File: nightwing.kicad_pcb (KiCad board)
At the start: 2 copper layers, 165.4 x 129.6 mm, 109 parts, among them J1 USB_C_Receptacle_USB2.0, J2 USB_C_Receptacle_USB2.0, J3 OLED, SW1 SW_PUSH, SW10 SW_PUSH, SW11 SW_PUSH, SW12 SW_PUSH, SW13 SW_PUSH, SW14 SW_PUSH, SW15 SW_PUSH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

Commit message: updated stm32
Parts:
- added G***: LOGO, private:tiny_nightwing, F.Cu at (37.1, 38.7)
- added G***: LOGO, private:icon_nightwing, F.Cu at (156.2, 87.4)
- added L40: WS2812B, reversible-kicad-footprints:ws2812_reversible, B.Cu at (86.9, 86.4)
- added L41: WS2812B, reversible-kicad-footprints:ws2812_reversible, B.Cu at (102.1, 31.0)
- added L42: WS2812B, reversible-kicad-footprints:ws2812_reversible, B.Cu at (66.0, 25.1)
- J2: moved to F.Cu
- moved RESET_SW1 33.5 mm to (139.6, 89.2)
- moved C1 28.1 mm to (149.1, 86.0), turned to 270 degrees
- moved R5 27.0 mm to (159.1, 81.5), turned to 0 degrees
- moved R7 25.8 mm to (159.1, 79.4), turned to 0 degrees
- moved C10 25.2 mm to (159.1, 77.3), turned to 0 degrees
- moved C5 20.4 mm to (136.2, 76.7), turned to 180 degrees
- moved R2 20.1 mm to (136.2, 72.6), turned to 0 degrees
- moved L37 17.6 mm to (150.0, 103.2)
- moved J2 13.5 mm to (171.8, 106.2), turned to 170 degrees
- moved U1 12.4 mm to (28.5, 26.8), turned to 180 degrees
- moved D23 11.7 mm to (136.7, 112.8)
- moved L16 11.7 mm to (85.5, 66.9)
- moved L17 11.7 mm to (104.5, 76.9)
- moved L18 11.7 mm to (123.5, 78.9)
- moved SW12 11.7 mm to (123.5, 65.4)
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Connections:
- L36 pad 4: Net-(L35-Pad2) -> Net-(L36-Pad4)
- U3 pad 1: BUZZER -> (no net)
- U3 pad 10: ROT_A -> (no net)
- U3 pad 11: ROT_B -> (no net)
- U3 pad 12: ROW3 -> (no net)
- U3 pad 21: Net-(U3-Pad21) -> (no net)
- U3 pad 22: Net-(U3-Pad22) -> WS_LED
- U3 pad 25: Net-(U3-Pad25) -> SK_LED
- U3 pad 26: Net-(U3-Pad26) -> ROW0
- U3 pad 27: Net-(U3-Pad27) -> ROW1
- U3 pad 28: Net-(U3-Pad28) -> ROW2
- U3 pad 29: Net-(U3-Pad29) -> COL5
- U3 pad 30: ROW0 -> COL4
- U3 pad 31: ROW1 -> COL3
- U3 pad 32: ROW2 -> COL2
- U3 pad 36: WS_LED -> BUZZER
- U3 pad 37: SK_LED -> COL1
- U3 pad 38: COL5 -> COL0
- U3 pad 39: COL4 -> ROT_A
- U3 pad 40: COL3 -> ROT_B
- U3 pad 41: COL2 -> ROW3
- U3 pad 42: Net-(U3-Pad42) -> (no net)
- U3 pad 8: COL1 -> (no net)
- U3 pad 9: COL0 -> (no net)
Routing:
- net Net-(L36-Pad4): track 0.00 -> 80.0 mm, vias 0 -> 3
- net +5V: track 983.4 -> 1041.2 mm, vias 38 -> 36
- net Net-(L41-Pad2): track 0.00 -> 42.7 mm, vias 0 -> 3
- net Net-(L35-Pad2): track 78.2 -> 43.8 mm, vias 2 -> 3
- net GND: track 143.7 -> 111.2 mm, vias 21 -> 88
- net Net-(L39-Pad2): track 3.85 -> 35.7 mm, vias 1 -> 2
- net ROW0: track 204.0 -> 176.9 mm
- net DP: track 177.1 -> 200.6 mm, vias 5 -> 3
- net RX: track 44.6 -> 66.6 mm
- net ROW1: track 180.1 -> 158.4 mm
- net RESET: track 57.1 -> 39.3 mm
- net DN: track 183.3 -> 199.0 mm, vias 5 -> 4
- net SCL: track 56.6 -> 42.3 mm
- net SDA: track 50.7 -> 38.9 mm, vias 1 -> 0
- net Net-(R2-Pad2): track 15.6 -> 4.47 mm, vias 2 -> 0
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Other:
- board size 165.4 x 129.6 mm -> 158.1 x 125.4 mm
- board text added: "Nightwing v1.0"

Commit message: updated final verseion
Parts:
- added G***: LOGO, DjinnFootprints:QMK_PoweredBy, B.Cu at (148.0, 89.7)
- added H1: MountingHole, MountingHole:MountingHole_2.2mm_M2_DIN965, F.Cu at (38.5, 62.5)
- added H10: MountingHole, MountingHole:MountingHole_2.2mm_M2_DIN965, F.Cu at (57.3, 86.0)
- added H2: MountingHole, MountingHole:MountingHole_2.2mm_M2_DIN965, F.Cu at (39.0, 81.5)
- added H3: MountingHole, MountingHole:MountingHole_2.2mm_M2_DIN965, F.Cu at (76.8, 44.2)
- added H4: MountingHole, MountingHole:MountingHole_2.2mm_M2_DIN965, F.Cu at (76.8, 62.9)
- added H5: MountingHole, MountingHole:MountingHole_2.2mm_M2_DIN965, F.Cu at (114.2, 55.0)
- added H6: MountingHole, MountingHole:MountingHole_2.2mm_M2_DIN965, F.Cu at (114.5, 74.2)
- added H7: MountingHole, MountingHole:MountingHole_2.2mm_M2_DIN965, F.Cu at (93.1, 89.3)
- added H8: MountingHole, MountingHole:MountingHole_2.2mm_M2_DIN965, F.Cu at (131.2, 100.9)
- added H9: MountingHole, MountingHole:MountingHole_2.2mm_M2_DIN965, F.Cu at (147.2, 130.7)
- added R1: 5.1k, Resistor_SMD:R_0805_2012Metric, F.Cu at (153.8, 83.0)
- added R6: 5.1k, Resistor_SMD:R_0805_2012Metric, F.Cu at (155.8, 83.0)
- added R8: 5.1k, Resistor_SMD:R_0805_2012Metric, F.Cu at (159.5, 75.5)
- added Ref**: Val**, private:nightwing_qmk, B.Cu at (148.1, 74.6)
- moved G*** 8.62 mm to (148.7, 91.5)
- moved C1 1.11 mm to (149.9, 85.2), turned to 0 degrees
- moved C2 1.05 mm to (146.4, 85.2), turned to 180 degrees
- moved C10 0.77 mm to (159.5, 78.0)
- moved R7 0.68 mm to (159.5, 80.0)
- moved R5 0.60 mm to (159.5, 82.0)
- moved G*** 0.43 mm to (36.7, 38.4)
- renumbered RESET_SW1 to RESET
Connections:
- U3 pad 8: (no net) -> SPLIT_HAND_PIN
- U3 pad 9: (no net) -> PLUG_DETECT
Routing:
- net +5V: track 1041.2 -> 1050.2 mm
- net SPLIT_HAND_PIN: track 0.00 -> 8.11 mm, vias 0 -> 2
- net GND: track 111.2 -> 116.6 mm, vias 88 -> 90
- net WS_LED: track 58.3 -> 62.4 mm
- net COL5: track 130.6 -> 126.7 mm
- net PLUG_DETECT: track 0.00 -> 3.07 mm
- net RX: track 66.6 -> 69.2 mm
- net RESET: track 39.3 -> 38.6 mm
- net DN: track 199.0 -> 198.4 mm
- net D+: track 7.89 -> 8.44 mm
- net D-: track 8.26 -> 8.82 mm
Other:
- board text removed: "Alexander Ding"

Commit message: final output jlcpcb
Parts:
- removed the G*** at (36.7, 38.4)
- removed the G*** at (148.0, 89.7)
- removed the G*** at (148.7, 91.5)
- removed H7: MountingHole, MountingHole:MountingHole_2.2mm_M2_DIN965
- added BOOT: SW_PUSH, reversible-kicad-footprints:SW_Push_1P1T_NO_6x6mm_H9.5mm, F.Cu at (155.4, 91.0)
- added G***: LOGO, private:nightwing_icon, B.Cu at (49.3, 38.1)
- added G***: LOGO, private:nightwing_icon, F.Cu at (35.6, 38.6)
- added Ref**: Val**, private:nightwing_text_small, B.Cu at (33.8, 43.7)
- added Ref**: Val**, private:qmk_logo, B.Cu at (33.9, 41.1)
- added Ref**: Val**, private:qmk_logo, F.Cu at (51.5, 41.1)
- added Ref**: Val**, private:nightwing_text_small, F.Cu at (51.7, 43.7)
- added Ref**: Val**, private:qmk_logo, B.Cu at (150.0, 90.4)
- moved H10 25.4 mm to (77.8, 101.0)
- moved Ref** 10.8 mm to (137.7, 77.5)
- moved D19 3.19 mm to (75.8, 106.7)
- moved RESET 1.80 mm to (139.5, 91.0)
- renumbered R1 to LEFT, R6 to RIGHT
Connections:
- U3 pad 10: (no net) -> BOOT
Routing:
- net BOOT: track 0.00 -> 29.3 mm, vias 0 -> 2
- net ROW3: track 133.3 -> 136.6 mm
- net Net-(D19-Pad2): track 5.89 -> 2.83 mm
- net PLUG_DETECT: track 3.07 -> 5.65 mm
- net RESET: track 38.6 -> 40.1 mm
- net +5V: track 1050.2 -> 1051.1 mm
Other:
- board text removed: "Nightwing v1.0"

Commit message: post fabrication
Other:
- board text added: "REDODER"
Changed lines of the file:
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@@
   (general
     (thickness 1.6)
-    (drawings 47)
+    (drawings 50)
     (tracks 1728)
     (zones 0)
@@
     (43 Eco2.User user hide)
     (44 Edge.Cuts user)
-    (45 Margin user hide)
+    (45 Margin user)
     (46 B.CrtYd user)
     (47 F.CrtYd user)
@@
     (pad_to_mask_clearance 0)
     (aux_axis_origin 19.645 101.135)
-    (visible_elements FFFFFF7F)
+    (visible_elements FFFFF77F)
     (pcbplotparams
-      (layerselection 0x3dc30_ffffffff)
+      (layerselection 0x3dcf0_ffffffff)
       (usegerberextensions false)
       (usegerberattributes true)
@@
       (drillshape 0)
       (scaleselection 1)
-      (outputdirectory "pos/"))
+      (outputdirectory "gerbers/"))
   )
   (net 0 "")
@@
       (effects (font (size 1 1) (thickness 0.15)))
     )
-    (fp_text user %R (at 0 0 90) (layer F.Fab)
-      (effects (font (size 0.5 0.5) (thickness 0.08)))
-    )
     (fp_line (start -1 0.625) (end -1 -0.625) (layer F.Fab) (width 0.1))
     (fp_line (start -1 -0.625) (end 1 -0.625) (layer F.Fab) (width 0.1))
@@
     (fp_line (start 1.68 -0.95) (end 1.68 0.95) (layer F.CrtYd) (width 0.05))
     (fp_line (start 1.68 0.95) (end -1.68 0.95) (layer F.CrtYd) (width 0.05))
+    (fp_text user %R (at 0 0 90) (layer F.Fab)
+      (effects (font (size 0.5 0.5) (thickness 0.08)))
+    )
     (fp_text user LEFT (at 0 -1.67 90) (layer B.SilkS)
       (effects (font (size 1 1) (thickness 0.15)) (justify mirror))
@@
       (effects (font (size 1 1) (thickness 0.15)))
     )
-    (fp_text user BOOT (at 0 4.11 180) (layer B.SilkS)
-      (effects (font (size 1 1) (thickness 0.15)) (justify mirror))
-    )
     (fp_circle (center 0 0) (end 1.75 -0.05) (layer F.Fab) (width 0.1))
     (fp_line (start -3.23 3.23) (end 3.23 3.23) (layer F.SilkS) (width 0.12))
@@
     (fp_line (start 3 -3) (end 3 3) (layer B.Fab) (width 0.1))
     (fp_line (start -3 3) (end -3 -3) (layer B.Fab) (width 0.1))
+    (fp_text user BOOT (at 0 4.11 180) (layer B.SilkS)
+      (effects (font (size 1 1) (thickness 0.15)) (justify mirror))
+    )
     (fp_text user %R (at 0 -4.05) (layer F.Fab)
       (effects (font (size 1 1) (thickness 0.15)))
@@
       (effects (font (size 1 1) (thickness 0.15)))
     )
-    (fp_text user RESET (at 0.01 4.24) (layer B.SilkS)
-      (effects (font (size 1 1) (thickness 0.15)) (justify mirror))
-    )
-    (fp_text user %R (at 0 -4.05) (layer F.Fab)
-      (effects (font (size 1 1) (thickness 0.15)))
-    )
     (fp_circle (center 0 0) (end 1.75 -0.05) (layer F.Fab) (width 0.1))
     (fp_line (start -3.23 3.23) (end 3.23 3.23) (layer F.SilkS) (width 0.12))
@@
     (fp_line (start 3 -3) (end 3 3) (layer B.Fab) (width 0.1))
     (fp_line (start -3 3) (end -3 -3) (layer B.Fab) (width 0.1))
+    (fp_text user RESET (at 0.01 4.24) (layer B.SilkS)
+      (effects (font (size 1 1) (thickness 0.15)) (justify mirror))
+    )
+    (fp_text user %R (at 0 -4.05) (layer F.Fab)
+      (effects (font (size 1 1) (thickness 0.15)))
+    )
     (pad 1 smd rect (at -3.975 -2.25) (size 1.55 1.3) (layers B.Cu B.Paste B.Mask)
       (net 96 RESET))
@@
       ))
   )
-  (gr_arc (start 78.626902 293.069794) (end 163.11 30.93869) (angle -24.72568529) (layer Edge.Cuts) (width 0.05))
-  (gr_arc (start 45.663001 19.298001) (end 45.327002 19.357) (angle -90) (layer Edge.Cuts) (width 0.05))
-  (gr_line (start 44.854998 16.052) (end 45.327002 19.357) (layer Edge.Cuts) (width 0.05))
+  (gr_line (start 14.85 20.954) (end 14.85 105.844) (layer Margin) (width 0.05))
+  (gr_arc (start 44.518999 16.110999) (end 44.854998 16.052) (angle -90) (layer Edge.Cuts) (width 0.05))
+  (gr_line (start 44.46 15.775) (end 33.924 17.254) (layer Edge.Cuts) (width 0.05))
   (gr_line (start 33.647 17.648998) (end 34.169034 20.923207) (layer Edge.Cuts) (width 0.05))
+  (gr_arc (start 33.982999 17.589999) (end 33.924 17.254) (angle -90) (layer Edge.Cuts) (width 0.05))
   (gr_arc (start 78.626902 293.069794) (end 19.645 24.050706) (angle 3.018307596) (layer Edge.Cuts) (width 0.05))
   (gr_arc (start 33.833035 20.982206) (end 33.892034 21.318205) (angle -90) (layer Edge.Cuts) (width 0.05))
-  (gr_arc (start 44.518999 16.110999) (end 44.854998 16.052) (angle -90) (layer Edge.Cuts) (width 0.05))
-  (gr_arc (start 33.982999 17.589999) (end 33.924 17.254) (angle -90) (layer Edge.Cuts) (width 0.05))
-  (gr_line (start 44.46 15.775) (end 33.924 17.254) (layer Edge.Cuts) (width 0.05))
-  (gr_arc (start 78.555309 293.064563) (end 14.85 20.954) (angle 31.64994468) (layer Margin) (width 0.05))
-  (gr_line (start 93.14 116.964) (end 53.17 116.964) (layer Margin) (width 0.05))
-  (gr_line (start 175.682 146.659) (end 182.428 104.758) (layer Margin) (width 0.05))
+  (gr_line (start 19.645 101.135) (end 19.645 24.050706) (layer Edge.Cuts) (width 0.05))
+  (gr_arc (start 78.626902 293.069794) (end 163.11 30.93869) (angle -24.72568529) (layer Edge.Cuts) (width 0.05))
+  (gr_arc (start 45.663001 19.298001) (end 45.327002 19.357) (angle -90) (layer Edge.Cuts) (width 0.05))
+  (gr_line (start 44.854998 16.052) (end 45.327002 19.357) (layer Edge.Cuts) (width 0.05))
   (gr_line (start 163.11 30.93869) (end 163.11 101.88) (layer Edge.Cuts) (width 0.05))
-  (gr_line (start 57.21 112.672) (end 57.21 101.135) (layer Edge.Cuts) (width 0.05))
+  (gr_line (start 177.74 104.41) (end 171.29 141.184) (layer Edge.Cuts) (width 0.05))
+  (gr_line (start 171.29 141.184) (end 115.57 131.334) (layer Edge.Cuts) (width 0.05))
   (gr_line (start 115.57 112.672) (end 115.57 131.334) (layer Edge.Cuts) (width 0.05))
-  (gr_line (start 19.645 101.135) (end 19.645 24.050706) (layer Edge.Cuts) (width 0.05))
-  (gr_arc (start 93.05 135.164) (end 93.05 116.964) (angle 90) (layer Margin) (width 0.05))
-  (gr_arc (start 42.05 116.964) (end 42.05 105.844) (angle 90) (layer Margin) (width 0.05))
   (gr_line (start 115.57 112.672) (end 57.21 112.672) (layer Edge.Cuts) (width 0.05))
   (gr_line (start 57.21 101.135) (end 19.645 101.135) (layer Edge.Cuts) (width 0.05))
+  (gr_line (start 163.11 101.88) (end 177.74 104.41) (layer Edge.Cuts) (width 0.05))
+  (gr_line (start 57.21 112.672) (end 57.21 101.135) (layer Edge.Cuts) (width 0.05))
+  (gr_arc (start 78.555309 293.064563) (end 14.85 20.954) (angle 13.1764542) (layer Margin) (width 0.05))
+  (gr_arc (start -180 105.844) (end 14.85 105.844) (angle -24.32194748) (layer Margin) (width 0.05))
+  (gr_arc (start 78.555309 293.064563) (end 167.11 27.997413) (angle -35.32074809) (layer Margin) (width 0.05))
+  (gr_text REDODER (at 148.427 95.82) (layer F.SilkS)
+    (effects (font (size 1.5 1.5) (thickness 0.3)))
+  )
+  (gr_line (start 93.14 116.964) (end 53.17 116.964) (layer Margin) (width 0.05))
+  (gr_line (start 175.682 146.659) (end 182.428 104.758) (layer Margin) (width 0.05))
+  (gr_arc (start 93.05 135.164) (end 93.05 116.964) (angle 90) (layer Margin) (width 0.05))
+  (gr_arc (start 42.05 116.964) (end 42.05 105.844) (angle 90) (layer Margin) (width 0.05))
   (gr_line (start 163.1 101.344) (end 182.428 104.758) (layer Margin) (width 0.05))
   (gr_line (start 11.68 11.9) (end 11.66 33.86) (layer Cmts.User) (width 0.15))
@@
   (gr_line (start 11.66 33.86) (end 33.74 33.86) (layer Cmts.User) (width 0.15))
   (gr_line (start 111.25 135.164) (end 175.682 146.659) (layer Margin) (width 0.05))
-  (gr_line (start 14.92 105.844) (end 42.04 105.844) (layer Margin) (width 0.05))
-  (gr_line (start 14.85 20.954) (end 14.85 105.16) (layer Margin) (width 0.05))
-  (gr_line (start 167.11 27.994) (end 167.11 101.334) (layer Margin) (width 0.05))
-  (gr_line (start 163.11 101.88) (end 177.74 104.41) (layer Edge.Cuts) (width 0.05))
-  (gr_line (start 177.74 104.41) (end 171.29 141.184) (layer Edge.Cuts) (width 0.05))
-  (gr_line (start 171.29 141.184) (end 115.57 131.334) (layer Edge.Cuts) (width 0.05))
+  (gr_line (start 14.85 105.844) (end 42.04 105.844) (layer Margin) (width 0.05))
+  (gr_line (start 167.11 27.997413) (end 167.11 101.334) (layer Margin) (width 0.05))
   (via (at 26.495 99.475) (size 0.6) (drill 0.3) (layers F.Cu B.Cu) (net 0))
   (segment (start 39.00812 23.121601) (end 38.833 21.702) (width 0.25) (layer B.Cu) (net 1))

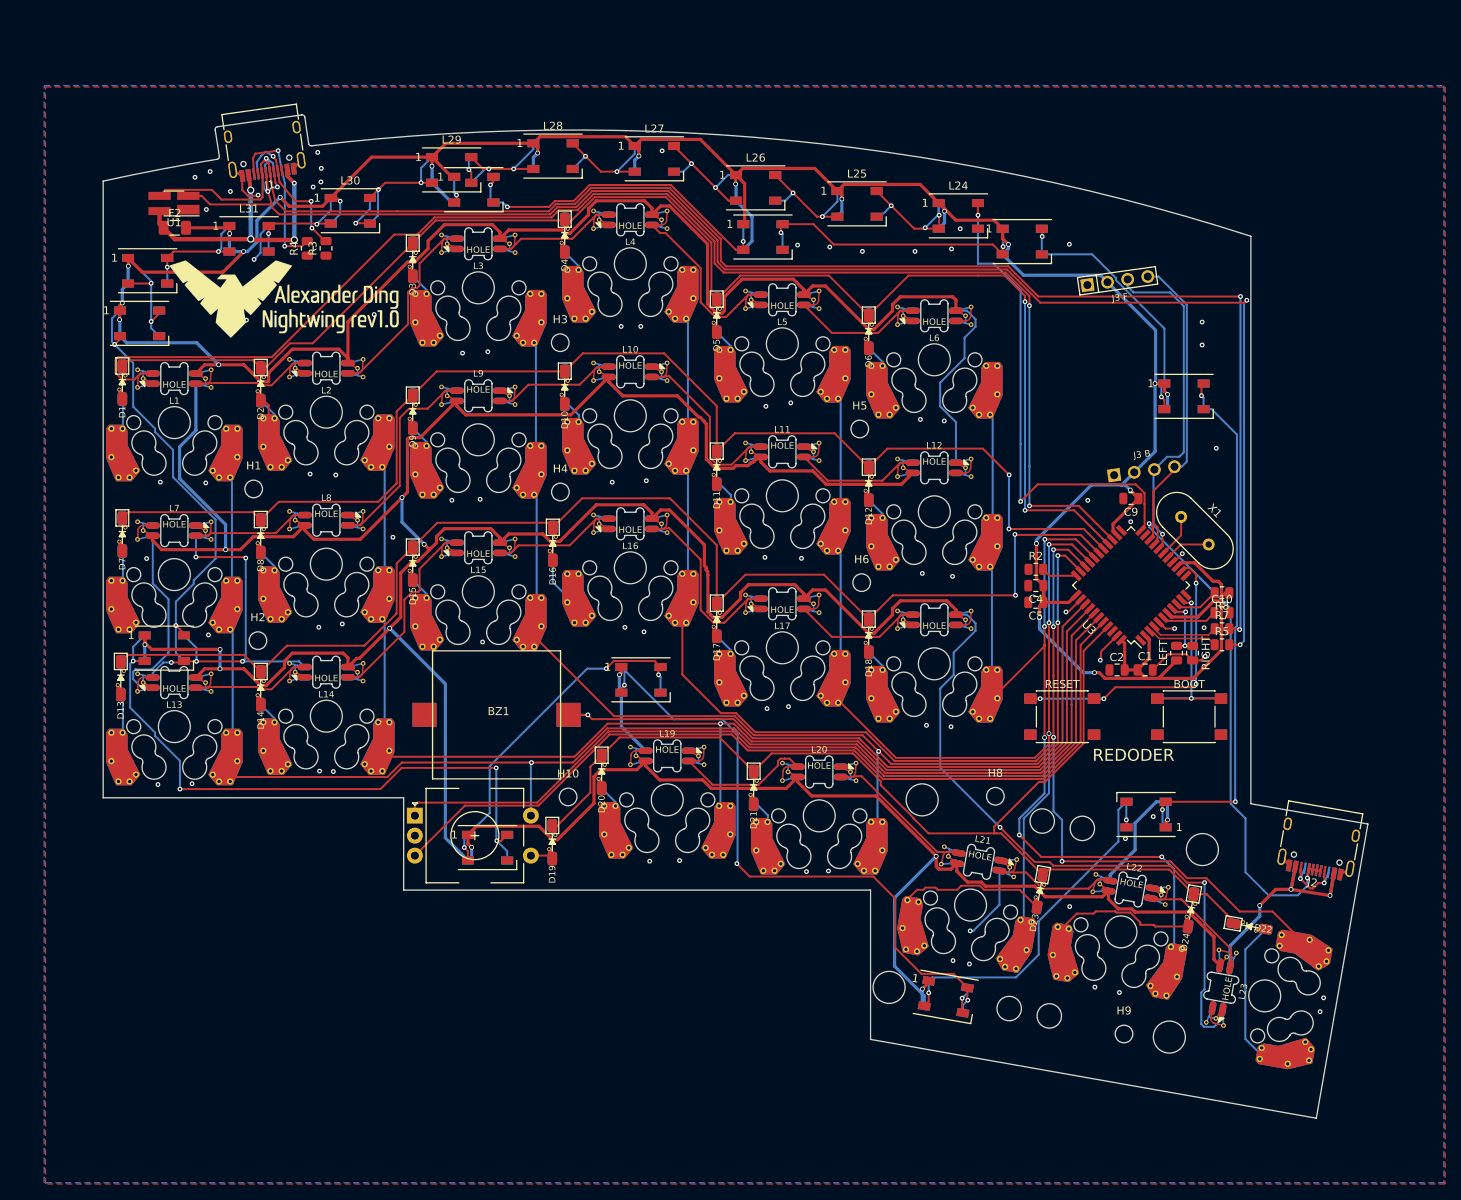
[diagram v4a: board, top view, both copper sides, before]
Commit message: fixed missing capactior
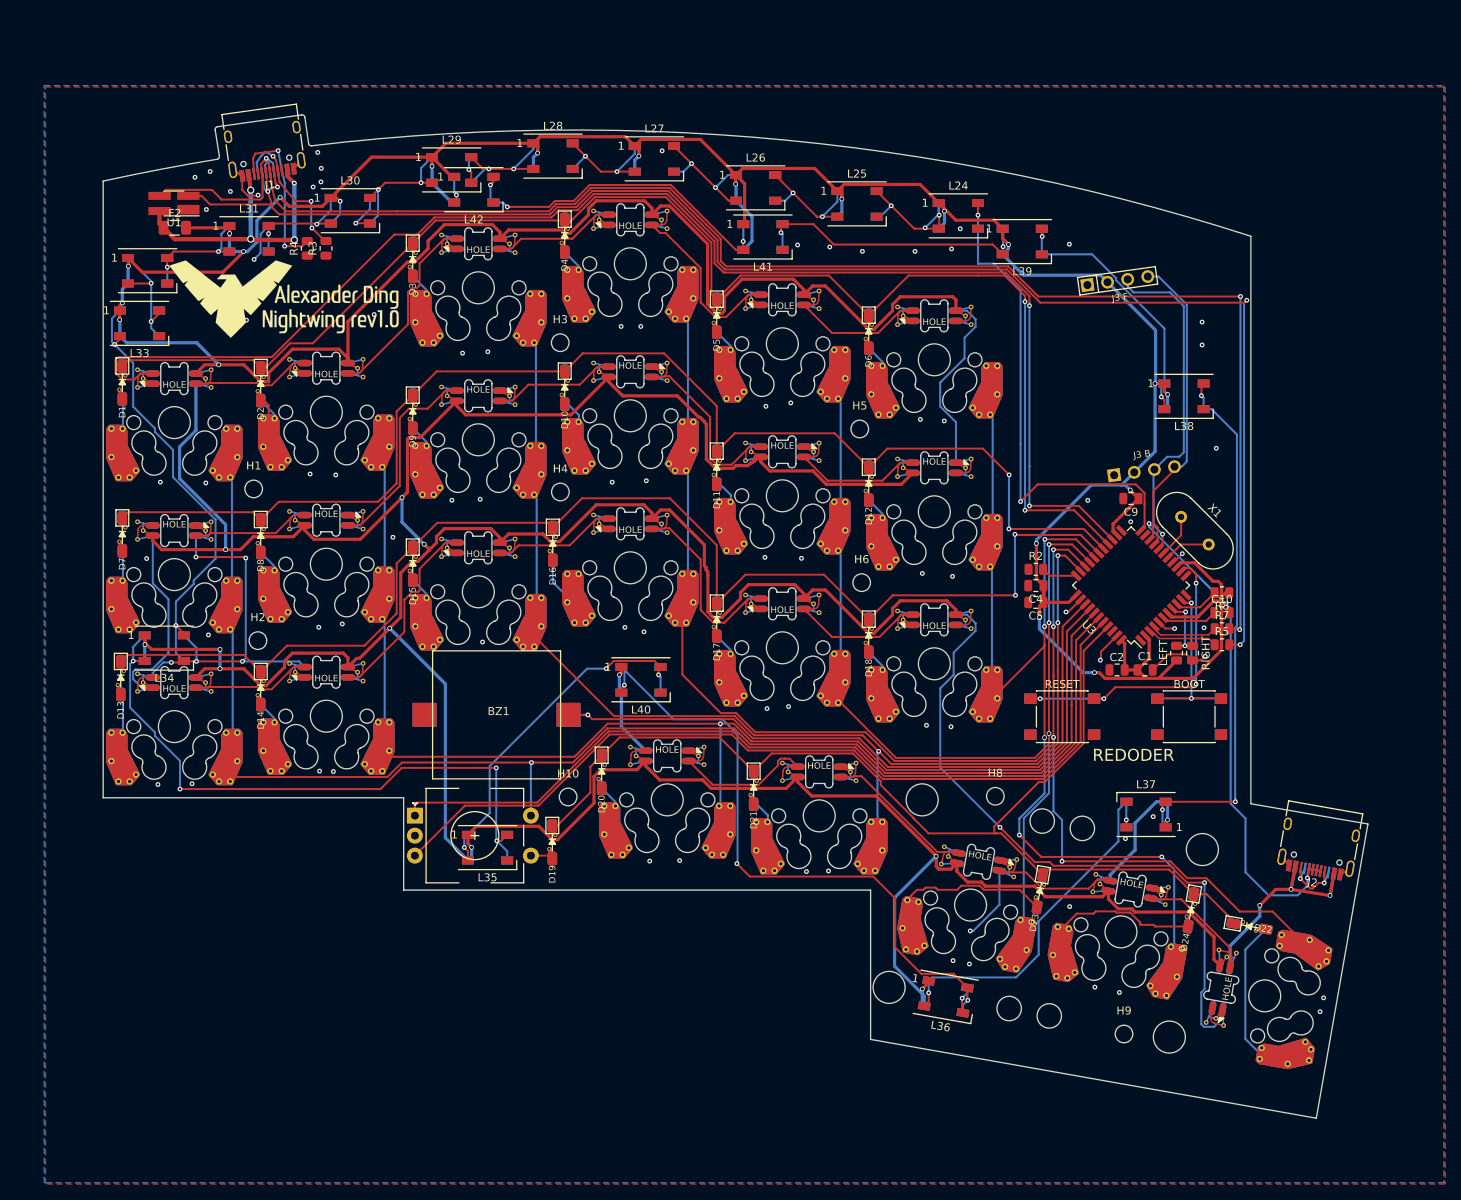
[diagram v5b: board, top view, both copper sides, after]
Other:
- net class Default removed
- net class Power removed
- net class Power 1.5A removed
- net class Power 3A removed
- net class Power Input removed
